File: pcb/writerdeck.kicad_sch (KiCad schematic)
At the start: 1 part, among them P1 USB_C_Plug

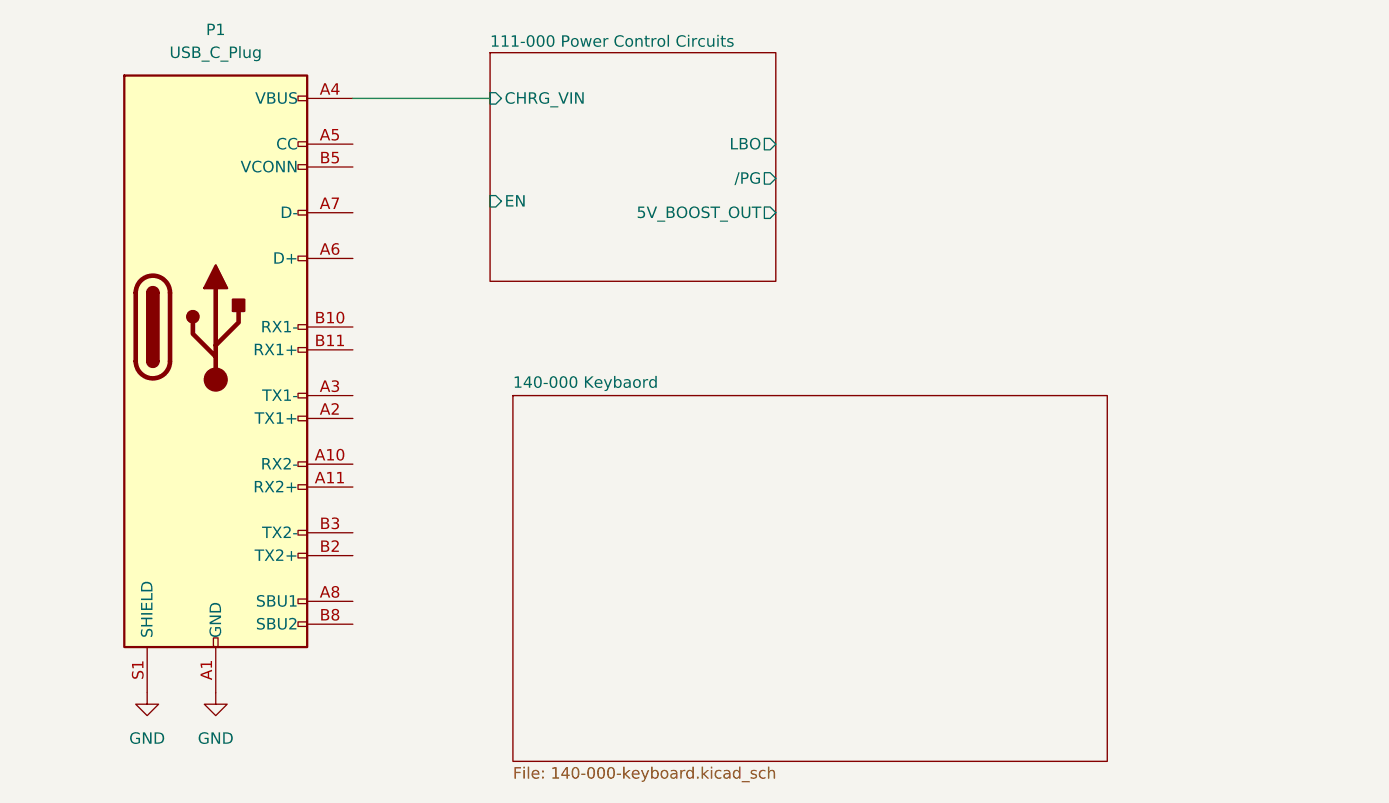
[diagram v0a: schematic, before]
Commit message: add keyboard
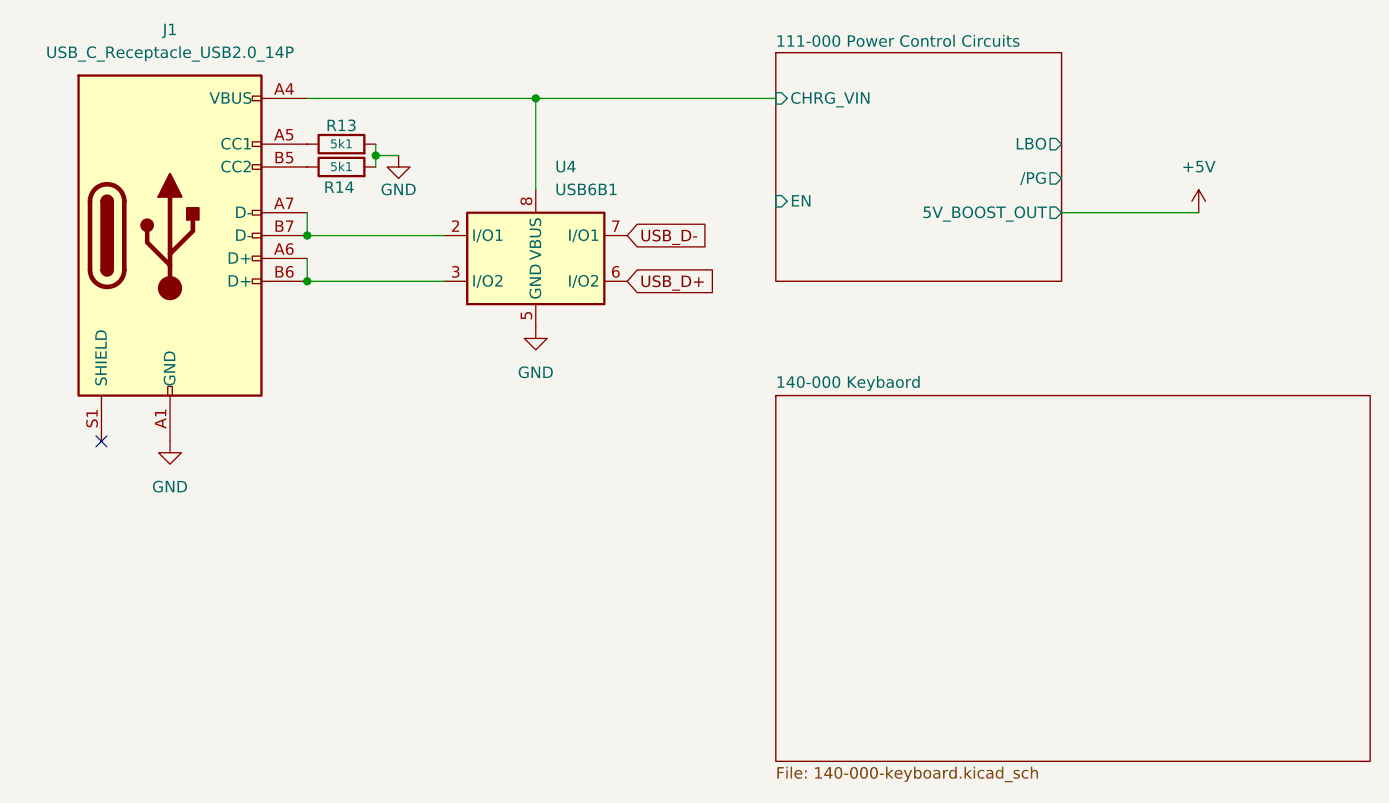
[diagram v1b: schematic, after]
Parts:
- removed P1: USB_C_Plug, symbol Connector:USB_C_Plug
- added J1: USB_C_Receptacle_USB2.0_14P, symbol Connector:USB_C_Receptacle_USB2.0_14P
- added R13, R14: 5k1, symbol Device:R
- added U4: USB6B1, Package_SO:SOIC-8_3.9x4.9mm_P1.27mm, symbol Power_Protection:USB6B1
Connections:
- net 111-000 Power Control Circuits/CHRG_VIN: now also J1.A4 (VBUS), J1.A9 (VBUS), J1.B4 (VBUS), J1.B9 (VBUS), U4.1 (VBUS), U4.8 (VBUS)
- net GND: now also J1.A1 (GND), J1.A12 (GND), J1.B1 (GND), J1.B12 (GND), R13.2, R14.2, U4.4 (GND), U4.5 (GND)
- new net: J1.A5 (CC1), R13.1
- new net: J1.B5 (CC2), R14.1
- new net: J1.A7 (D-), J1.B7 (D-), U4.2 (I/O1)
- new net: J1.A6 (D+), J1.B6 (D+), U4.3 (I/O2)
- new net USB_D+: U4.6 (I/O2)
- new net USB_D-: U4.7 (I/O1)
- no-connect marks 0 -> 1

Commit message: add rp2040 datasheet, and add rp2040 to keyboard unconnected
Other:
- note added: "Charging and interface usb"
- note added: "ESD Protection Circuit"
- note added: "Pull this low to disconnect output and turn off downstream"
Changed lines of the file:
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@@
 		(rev "1")
+	)
+	(text "Charging and interface usb"
+		(exclude_from_sim no)
+		(at 49.784 68.326 0)
+		(effects
+			(font
+				(size 1 1)
+			)
+		)
+	)
+	(text "ESD Protection Circuit"
+		(exclude_from_sim no)
+		(at 87.376 58.674 0)
+		(effects
+			(font
+				(size 1 1)
+			)
+		)
+	)
+	(text "Pull this low to \ndisconnect output \nand turn off downstream"
+		(exclude_from_sim no)
+		(at 103.632 48.514 0)
+		(effects
+			(font
+				(size 1 1)
+			)
+			(justify left)
+		)
 	)
 	(junction

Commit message: major keyboard components completed
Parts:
- R13, R14: footprint (none) -> Resistor_SMD:R_0402_1005Metric
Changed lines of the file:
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@@
 			)
 		)
-		(property "Footprint" ""
+		(property "Footprint" "Resistor_SMD:R_0402_1005Metric"
 			(at 54.61 39.878 90)
 			(effects
@@
 			)
 		)
-		(property "Footprint" ""
+		(property "Footprint" "Resistor_SMD:R_0402_1005Metric"
 			(at 54.61 42.418 90)
 			(effects
